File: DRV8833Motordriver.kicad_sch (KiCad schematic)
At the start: 8 parts, among them J1 Conn_01x06_Pin, J2 Conn_01x06_Pin, U1 DRV8833PWP

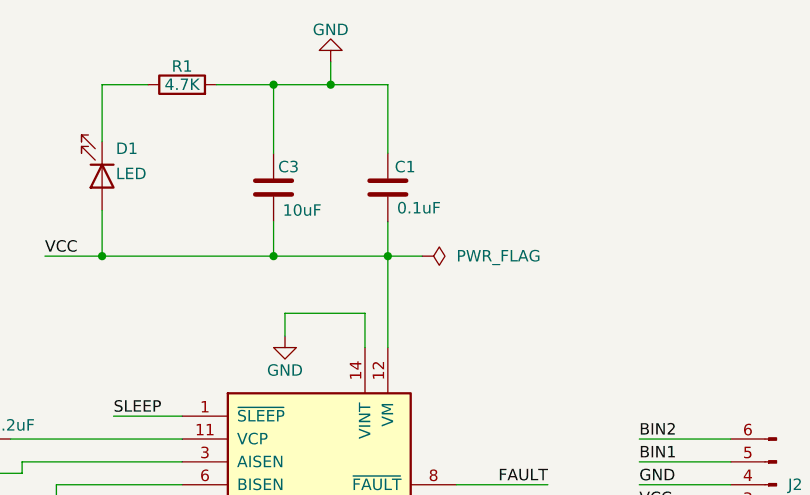
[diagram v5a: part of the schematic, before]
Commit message: Changed C3 to Unpolarized Capacitor
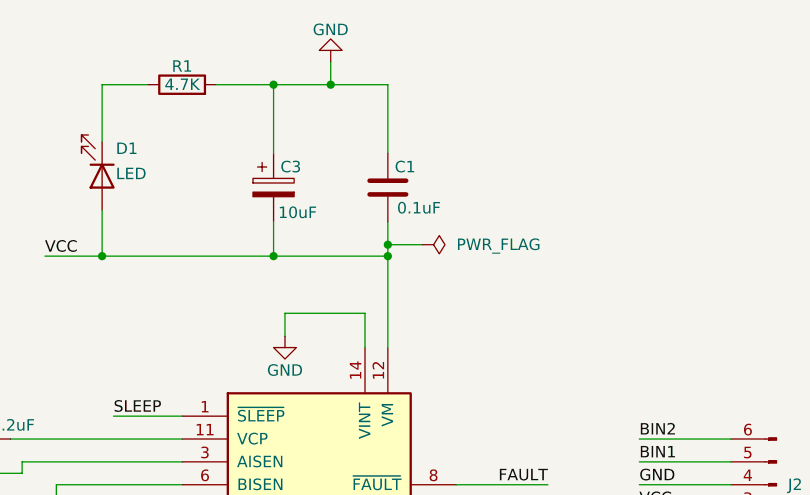
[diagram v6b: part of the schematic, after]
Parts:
- removed C3: 10uF, Capacitor_Tantalum_SMD:CP_EIA-6032-20_AVX-F, symbol Device:C
- added C3: 10uF, Capacitor_Tantalum_SMD:CP_EIA-6032-20_AVX-F, symbol Device:C_Polarized
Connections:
- net GND: now also C3.1
- net VCC: now also C3.2
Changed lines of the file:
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@@
 	(paper "A4")
+	(junction
+		(at 105.41 93.98)
+		(diameter 0)
+		(color 0 0 0 0)
+	)
+	(junction
+		(at 127 69.85)
+		(diameter 0)
+		(color 0 0 0 0)
+	)
+	(junction
+		(at 158.75 68.58)
+		(diameter 0)
+		(color 0 0 0 0)
+	)
+	(junction
+		(at 152.4 50.8)
+		(diameter 0)
+		(color 0 0 0 0)
+	)
+	(junction
+		(at 146.05 69.85)
+		(diameter 0)
+		(color 0 0 0 0)
+	)
 	(junction
 		(at 158.75 69.85)
@@
 	)
 	(junction
-		(at 105.41 93.98)
-		(diameter 0)
-		(color 0 0 0 0)
-	)
-	(junction
-		(at 127 69.85)
-		(diameter 0)
-		(color 0 0 0 0)
-	)
-	(junction
-		(at 152.4 50.8)
-		(diameter 0)
-		(color 0 0 0 0)
-	)
-	(junction
-		(at 146.05 69.85)
-		(diameter 0)
-		(color 0 0 0 0)
-	)
-	(junction
 		(at 146.05 50.8)
 		(diameter 0)
@@
 	(wire
 		(pts
+			(xy 158.75 69.85) (xy 158.75 80.01)
+		)
+		(stroke
+			(width 0)
+			(type default)
+		)
+	)
+	(wire
+		(pts
 			(xy 105.41 90.17) (xy 109.22 90.17)
 		)
@@
 	(wire
 		(pts
-			(xy 158.75 69.85) (xy 158.75 80.01)
-		)
-		(stroke
-			(width 0)
-			(type default)
-		)
-	)
-	(wire
-		(pts
 			(xy 152.4 48.26) (xy 152.4 50.8)
 		)
@@
 	(wire
 		(pts
+			(xy 158.75 68.58) (xy 158.75 69.85)
+		)
+		(stroke
+			(width 0)
+			(type default)
+		)
+	)
+	(wire
+		(pts
 			(xy 105.41 93.98) (xy 105.41 96.52)
 		)
@@
 	(wire
 		(pts
-			(xy 158.75 69.85) (xy 162.56 69.85)
-		)
-		(stroke
-			(width 0)
-			(type default)
-		)
-	)
-	(wire
-		(pts
 			(xy 81.28 96.52) (xy 93.98 96.52)
 		)
@@
 	(wire
 		(pts
-			(xy 158.75 66.04) (xy 158.75 69.85)
+			(xy 158.75 66.04) (xy 158.75 68.58)
 		)
 		(stroke
@@
 		(pts
 			(xy 166.37 95.25) (xy 176.53 95.25)
+		)
+		(stroke
+			(width 0)
+			(type default)
+		)
+	)
+	(wire
+		(pts
+			(xy 158.75 68.58) (xy 162.56 68.58)
 		)
 		(stroke
@@
 	(symbol
 		(lib_id "power:PWR_FLAG")
-		(at 162.56 69.85 270)
+		(at 162.56 68.58 270)
 		(unit 1)
 		(exclude_from_sim no)
@@
 		(fields_autoplaced yes)
 		(property "Reference" "#FLG02"
-			(at 164.465 69.85 0)
+			(at 164.465 68.58 0)
 			(effects
 				(font
@@
 		)
 		(property "Value" "PWR_FLAG"
-			(at 166.37 69.8499 90)
+			(at 166.37 68.5799 90)
 			(effects
 				(font
@@
 		)
 		(property "Footprint" ""
-			(at 162.56 69.85 0)
+			(at 162.56 68.58 0)
 			(effects
 				(font
@@
 		)
 		(property "Datasheet" "~"
-			(at 162.56 69.85 0)
+			(at 162.56 68.58 0)
 			(effects
 				(font
@@
 		)
 		(property "Description" "Special symbol for telling ERC where power comes from"
-			(at 162.56 69.85 0)
+			(at 162.56 68.58 0)
 			(effects
 				(font
@@
 	)
 	(symbol
-		(lib_id "Device:C")
+		(lib_id "Device:C_Polarized")
 		(at 146.05 62.23 0)
 		(unit 1)
@@
 		(dnp no)
 		(property "Reference" "C3"
-			(at 146.558 59.944 0)
+			(at 146.812 59.944 0)
 			(effects
 				(font
@@
 		)
 		(property "Value" "10uF"
-			(at 147.066 64.77 0)
+			(at 146.558 65.024 0)
 			(effects
 				(font
@@
 			)
 		)
-		(property "Description" "Unpolarized capacitor"
+		(property "Description" "Polarized capacitor"
 			(at 146.05 62.23 0)
 			(effects
@@
 			)
 		)
+		(pin "2"
+		)
 		(pin "1"
 		)
-		(pin "2"
-		)
 		(instances
-			(project "DRV8833Motordriver"
+			(project ""
 				(path "/73ddca82-4703-47cd-ad38-0c288e172b95"
 					(reference "C3")
